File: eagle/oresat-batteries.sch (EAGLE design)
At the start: 308 parts, among them J1 J-SAMTEC-TFM-120-X1-XXX-D-RA, J4 ORESAT-DEBUG-CONNECTOR-ALL, Q1 DMP2240UDM, Q10 NTR4101, Q11 PMV45EN, Q12 Si7625DN, Q13 Si7625DN, Q14 NTR4101, Q15 NTR4101, Q16 Si7625DN, Q17 Si7625DN, Q18 Si7625DN, Q19 Si7625DN, Q2 PMV45EN, Q22 PMV45EN, Q23 NTR4101, Q24 PM45VEN, Q25 PM45VEN, Q26 PM45VEN, Q27 PM45VEN, Q28 NTR4101, Q29 PM45VEN, Q3 DMP3050LVT-7, Q30 Si7625DN, Q31 Si7625DN, Q32 NTR4101, Q33 NTR4101, Q34 Si7625DN, Q35 Si7625DN, Q36 Si7625DN, Q37 Si7625DN, Q4 DMP3050LVT-7, Q40 PM45VEN, Q41 NTR4101, Q42 DMP2240UDM, Q43 DMP2240UDM, Q44 PMV45EN, Q45 FDMQ86530L_2-GATES, Q5 PMV45EN, Q6 PM45VEN, Q7 PM45VEN, Q8 PM45VEN, Q9 PM45VEN, U1 MAX7310ATE, U10 LTC4412, U11 LTC4412, U12 MAX17205G, U13 S-8209AAA-T8T1U, U14 S-8209AAA-T8T1U, U15 LTC4412, U16 LTC4412, U17 MAX17205G, U2 MIC842LYC5, U20 TCAN330, U21 STM32F091C, U3 MIC842LYC5, U4 MAX4211FETE, U5 TPS62111RSA, U8 S-8209AAA-T8T1U, U9 S-8209AAA-T8T1U, X3 16MHZ-2.5x2mm

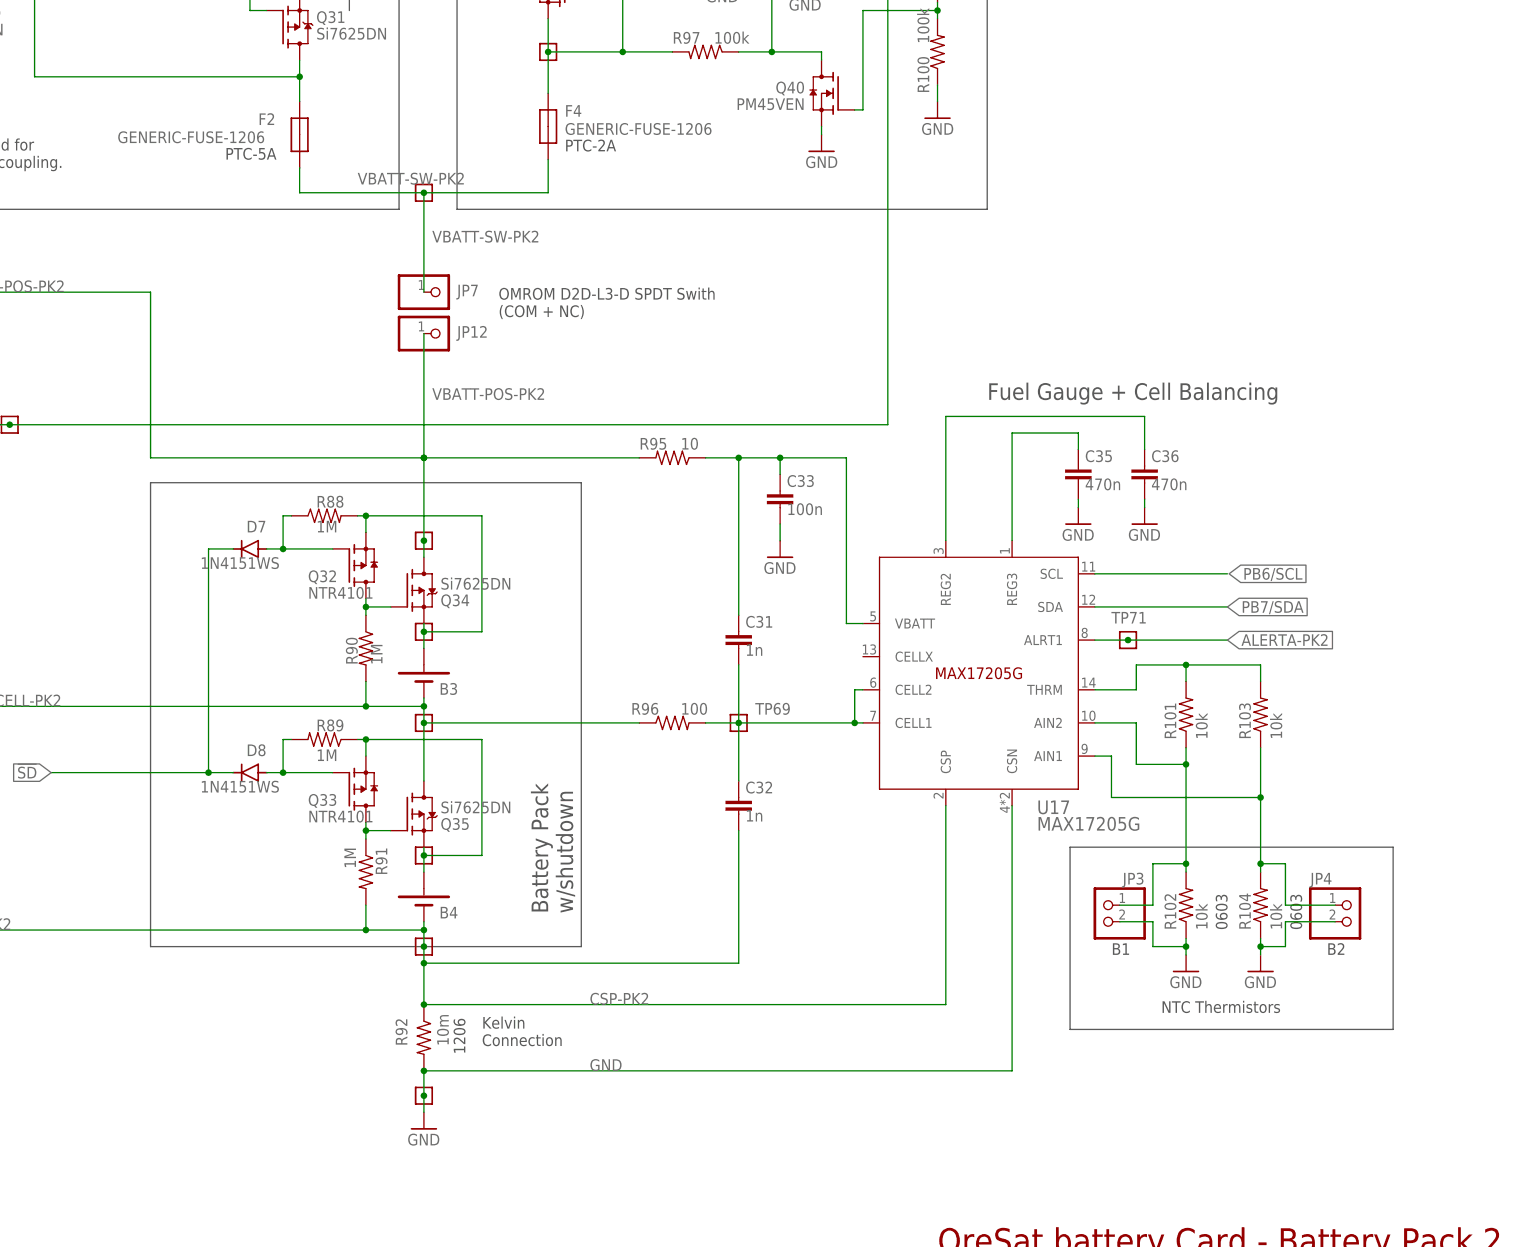
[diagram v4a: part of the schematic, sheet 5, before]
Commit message: Full update of the BOM; added non PCB materials including the heaters, thermistors. Updated fuses to be decent PTCs. Might regret that later, but it really seems like the right thing.
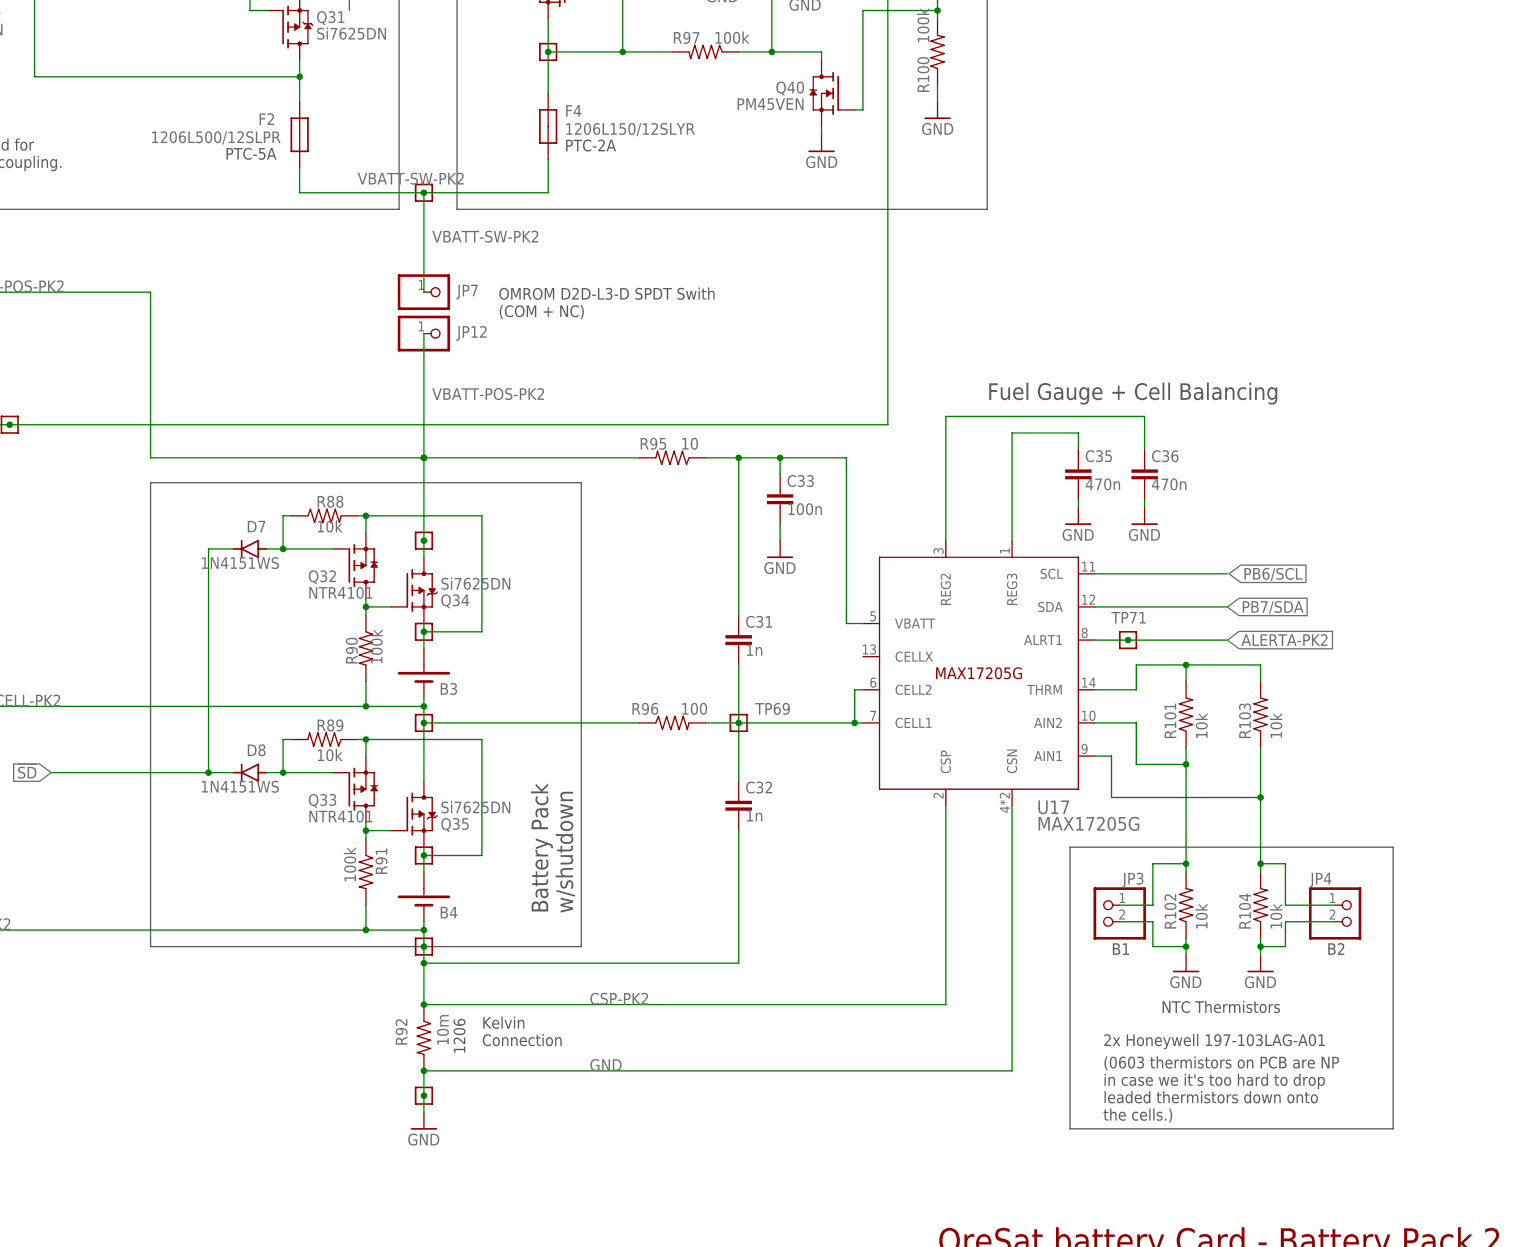
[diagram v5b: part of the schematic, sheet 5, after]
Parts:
- C7: value NP -> 1u
- F1, F2: value GENERIC-FUSE-1206 -> 1206L500/12SLPR
- F3, F4: value GENERIC-FUSE-1206 -> 1206L150/12SLYR
- R26: value NP -> 100k
- R27: value NP -> 10k
- R88, R89: value 1M -> 10k
- R90, R91: value 1M -> 100k
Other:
- note added: "(0603 thermistors on PCB are NP in case we it's too hard to drop leaded thermistors down onto the cells.)"
- note added: "2x Honeywell 197-103LAG-A01"
- note removed: "0603"
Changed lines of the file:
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@@
 <part name="TP41" library="oresat-misc" deviceset="TEST-POINT-LARGE-SQUARE" device=""/>
 <part name="TP39" library="oresat-misc" deviceset="TEST-POINT-LARGE-SQUARE" device=""/>
-<part name="F1" library="F-Generic-Fuse-1206" deviceset="GENERIC-FUSE-1206" device="">
+<part name="F1" library="F-Generic-Fuse-1206" deviceset="GENERIC-FUSE-1206" device="" value="1206L500/12SLPR">
 <attribute name="DIS" value="Digi-Key"/>
 <attribute name="DPN" value="F9966CT-ND"/>
@@
 <attribute name="MPN" value="S-8209AAA-T8T1U"/>
 </part>
-<part name="R91" library="oresat-rcl" deviceset="R-US_" device="0603-C-NOSILK" value="1M">
+<part name="R91" library="oresat-rcl" deviceset="R-US_" device="0603-C-NOSILK" value="100k">
 <attribute name="DIS" value="Digi-Key"/>
 <attribute name="DPN" value="311-1.00MHRCT-ND"/>
@@
 <attribute name="MPN" value="RC0603FR-071ML"/>
 </part>
-<part name="R90" library="oresat-rcl" deviceset="R-US_" device="0603-C-NOSILK" value="1M">
+<part name="R90" library="oresat-rcl" deviceset="R-US_" device="0603-C-NOSILK" value="100k">
 <attribute name="DIS" value="Digi-Key"/>
 <attribute name="DPN" value="311-1.00MHRCT-ND"/>
@@
 <attribute name="MPN" value="1N4151WS-E3-08"/>
 </part>
-<part name="R89" library="oresat-rcl" deviceset="R-US_" device="0603-C-NOSILK" value="1M">
+<part name="R89" library="oresat-rcl" deviceset="R-US_" device="0603-C-NOSILK" value="10k">
 <attribute name="DIS" value="Digi-Key"/>
 <attribute name="DPN" value="311-1.00MHRCT-ND"/>
@@
 <attribute name="MPN" value="RC0603FR-071ML"/>
 </part>
-<part name="R88" library="oresat-rcl" deviceset="R-US_" device="0603-C-NOSILK" value="1M">
+<part name="R88" library="oresat-rcl" deviceset="R-US_" device="0603-C-NOSILK" value="10k">
 <attribute name="DIS" value="Digi-Key"/>
 <attribute name="DPN" value="311-1.00MHRCT-ND"/>
@@
 <part name="TP64" library="oresat-misc" deviceset="TEST-POINT-LARGE-SQUARE" device=""/>
 <part name="TP62" library="oresat-misc" deviceset="TEST-POINT-LARGE-SQUARE" device=""/>
-<part name="F2" library="F-Generic-Fuse-1206" deviceset="GENERIC-FUSE-1206" device="">
+<part name="F2" library="F-Generic-Fuse-1206" deviceset="GENERIC-FUSE-1206" device="" value="1206L500/12SLPR">
 <attribute name="DIS" value="Digi-Key"/>
 <attribute name="DPN" value="F9966CT-ND"/>
@@
 <attribute name="MPN" value="RC0603FR-0710KL"/>
 </part>
-<part name="R26" library="oresat-rcl" deviceset="R-US_" device="0603-C-NOSILK" value="NP">
+<part name="R26" library="oresat-rcl" deviceset="R-US_" device="0603-C-NOSILK" value="100k">
 <attribute name="DIS" value="Digi-Key"/>
 <attribute name="DPN" value="1276-4275-1-ND"/>
@@
 <attribute name="MPN" value="RC1005F6653CS"/>
 </part>
-<part name="R27" library="oresat-rcl" deviceset="R-US_" device="0603-C-NOSILK" value="NP">
+<part name="R27" library="oresat-rcl" deviceset="R-US_" device="0603-C-NOSILK" value="10k">
 <attribute name="DIS" value="Digi-Key"/>
 <attribute name="DPN" value="1276-4275-1-ND"/>
@@
 </part>
 <part name="GND19" library="supply1" library_urn="urn:adsk.eagle:library:371" deviceset="GND" device=""/>
-<part name="C7" library="oresat-rcl" deviceset="C-EU" device="0603-C-NOSILK" value="NP"/>
+<part name="C7" library="oresat-rcl" deviceset="C-EU" device="0603-C-NOSILK" value="1u"/>
 <part name="GND28" library="supply1" library_urn="urn:adsk.eagle:library:371" deviceset="GND" device=""/>
 <part name="R38" library="oresat-rcl" deviceset="R-US_" device="0603-C-NOSILK" value="10k">
@@
 <part name="GND31" library="supply1" library_urn="urn:adsk.eagle:library:371" deviceset="GND" device=""/>
 <part name="GND32" library="supply1" library_urn="urn:adsk.eagle:library:371" deviceset="GND" device=""/>
-<part name="F3" library="F-Generic-Fuse-1206" deviceset="GENERIC-FUSE-1206" device="">
+<part name="F3" library="F-Generic-Fuse-1206" deviceset="GENERIC-FUSE-1206" device="" value="1206L150/12SLYR">
 <attribute name="DIS" value="Digi-Key"/>
 <attribute name="DPN" value="F9966CT-ND"/>
@@
 </part>
 <part name="PCB1" library="oresat-cards" deviceset="ORESAT-CARD-V1.3-BATTERY" device=""/>
-<part name="F4" library="F-Generic-Fuse-1206" deviceset="GENERIC-FUSE-1206" device="">
+<part name="F4" library="F-Generic-Fuse-1206" deviceset="GENERIC-FUSE-1206" device="" value="1206L150/12SLYR">
 <attribute name="DIS" value="Digi-Key"/>
 <attribute name="DPN" value="F9966CT-ND"/>
@@
 <text x="267.97" y="30.48" size="1.778" layer="97" rot="R270">-Y HEATER</text>
 <text x="288.29" y="31.75" size="1.778" layer="97" rot="R270">+Y HEATER</text>
-<text x="232.41" y="12.7" size="1.778" layer="97">2x Minco HK6903 Heaters (12.7 x 101.6 mm @ 49 ohm)</text>
+<text x="247.65" y="12.7" size="1.778" layer="97">2x Minco HK6903 Heaters (12.7 x 101.6 mm @ 49 ohm)</text>
 <wire x1="275.59" y1="52.07" x2="262.89" y2="52.07" width="0.1524" layer="97"/>
 <wire x1="262.89" y1="52.07" x2="262.89" y2="16.51" width="0.1524" layer="97"/>
@@
 <wire x1="214.63" y1="73.66" x2="280.67" y2="73.66" width="0.1524" layer="97"/>
 <text x="262.89" y="55.88" size="1.778" layer="97" rot="R90">1206</text>
-<text x="391.16" y="76.2" size="1.778" layer="97" rot="R90">0603</text>
-<text x="379.73" y="76.2" size="1.778" layer="97" rot="R90">0603</text>
-<wire x1="355.6" y1="88.9" x2="355.6" y2="60.96" width="0.1524" layer="97"/>
-<wire x1="355.6" y1="60.96" x2="405.13" y2="60.96" width="0.1524" layer="97"/>
-<wire x1="405.13" y1="60.96" x2="405.13" y2="88.9" width="0.1524" layer="97"/>
+<wire x1="355.6" y1="88.9" x2="355.6" y2="44.45" width="0.1524" layer="97"/>
+<wire x1="355.6" y1="44.45" x2="405.13" y2="44.45" width="0.1524" layer="97"/>
+<wire x1="405.13" y1="44.45" x2="405.13" y2="88.9" width="0.1524" layer="97"/>
 <wire x1="405.13" y1="88.9" x2="355.6" y2="88.9" width="0.1524" layer="97"/>
 <text x="369.57" y="63.5" size="1.778" layer="97">NTC Thermistors </text>
@@
 <text x="266.7" y="166.37" size="1.778" layer="97">OMRON D2D-L3-D SPDT Switch
 (COM + NC)</text>
+<text x="360.68" y="46.99" size="1.778" layer="97">(0603 thermistors on PCB are NP
+in case we it's too hard to drop
+leaded thermistors down onto
+the cells.)</text>
+<text x="360.68" y="59.69" size="1.778" layer="97">2x Honeywell 197-103LAG-A01</text>
 </plain>
 <instances>
@@
 <instance part="F1" gate="G$1" x="237.49" y="198.12" smashed="yes" rot="R90">
 <attribute name="NAME" x="232.41" y="200.66" size="1.778" layer="95"/>
-<attribute name="VALUE" x="210.82" y="197.358" size="1.778" layer="96"/>
+<attribute name="VALUE" x="214.63" y="197.358" size="1.778" layer="96"/>
 <attribute name="DPN" x="237.49" y="198.12" size="1.778" layer="96" rot="R90" display="off"/>
 <attribute name="MFR" x="237.49" y="198.12" size="1.778" layer="96" rot="R90" display="off"/>
@@
 <wire x1="214.63" y1="73.66" x2="280.67" y2="73.66" width="0.1524" layer="97"/>
 <text x="262.89" y="57.15" size="1.778" layer="97" rot="R90">1206</text>
-<text x="391.16" y="76.2" size="1.778" layer="97" rot="R90">0603</text>
-<text x="379.73" y="76.2" size="1.778" layer="97" rot="R90">0603</text>
-<wire x1="355.6" y1="88.9" x2="355.6" y2="60.96" width="0.1524" layer="97"/>
-<wire x1="355.6" y1="60.96" x2="405.13" y2="60.96" width="0.1524" layer="97"/>
-<wire x1="405.13" y1="60.96" x2="405.13" y2="88.9" width="0.1524" layer="97"/>
+<wire x1="355.6" y1="88.9" x2="355.6" y2="45.72" width="0.1524" layer="97"/>
+<wire x1="355.6" y1="45.72" x2="405.13" y2="45.72" width="0.1524" layer="97"/>
+<wire x1="405.13" y1="45.72" x2="405.13" y2="88.9" width="0.1524" layer="97"/>
 <wire x1="405.13" y1="88.9" x2="355.6" y2="88.9" width="0.1524" layer="97"/>
 <text x="369.57" y="63.5" size="1.778" layer="97">NTC Thermistors </text>
@@
 <text x="267.97" y="170.18" size="1.778" layer="97">OMROM D2D-L3-D SPDT Swith
 (COM + NC)</text>
+<text x="360.68" y="46.99" size="1.778" layer="97">(0603 thermistors on PCB are NP
+in case we it's too hard to drop
+leaded thermistors down onto
+the cells.)</text>
+<text x="360.68" y="58.42" size="1.778" layer="97">2x Honeywell 197-103LAG-A01</text>
 </plain>
 <instances>
@@
 <instance part="F2" gate="G$1" x="237.49" y="198.12" smashed="yes" rot="R90">
 <attribute name="NAME" x="231.14" y="199.6186" size="1.778" layer="95"/>
-<attribute name="VALUE" x="209.55" y="196.85" size="1.778" layer="96"/>
+<attribute name="VALUE" x="214.63" y="196.85" size="1.778" layer="96"/>
 <attribute name="MPN" x="237.49" y="198.12" size="1.778" layer="96" rot="R90" display="off"/>
 <attribute name="DPN" x="237.49" y="198.12" size="1.778" layer="96" rot="R90" display="off"/>

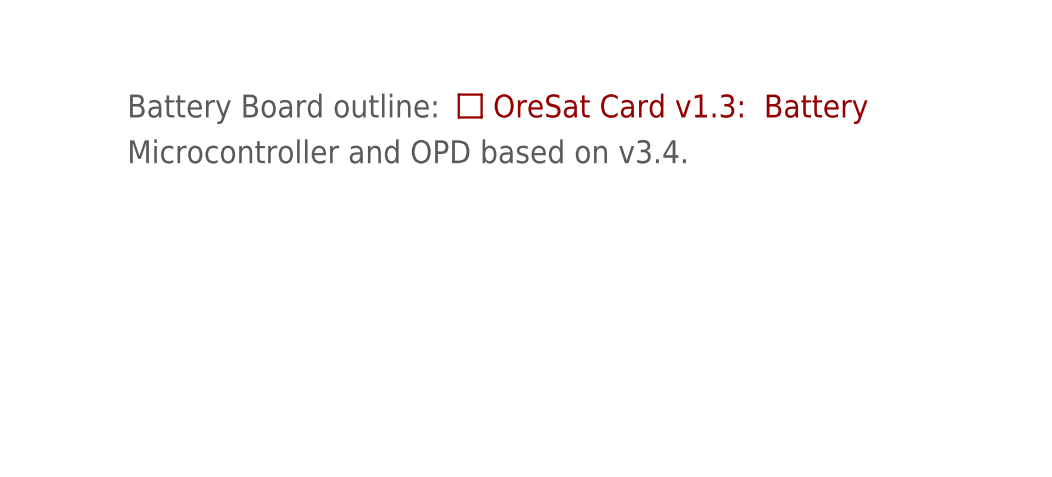
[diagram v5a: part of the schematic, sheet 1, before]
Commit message: Upped battery board to v2.1. No real changes, besides adding fiducials (blargh!), updating the board version, and adding the flight marker to TPLACE.
More importantly, the BOM has been upadated to reflect what Screaming Circuits is going to stuff for us.
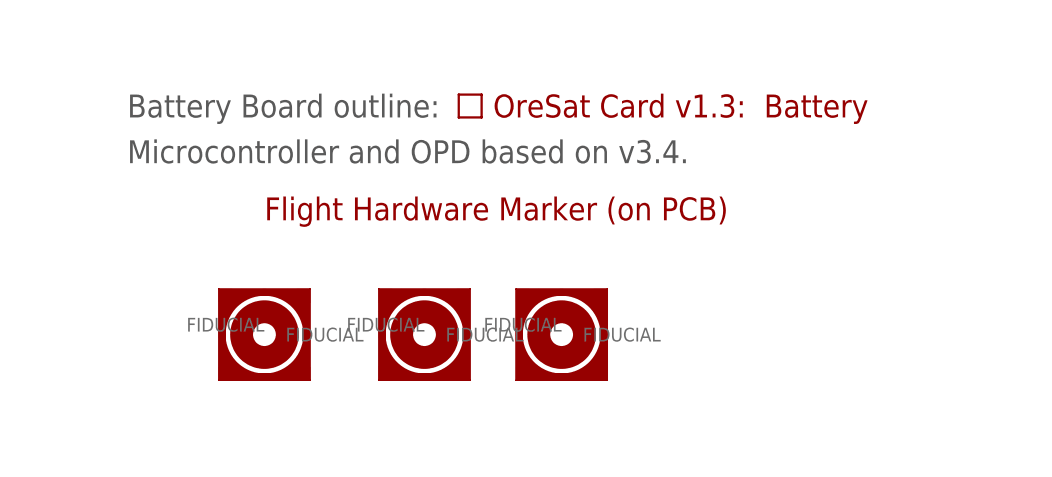
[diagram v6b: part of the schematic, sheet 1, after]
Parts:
- added FIDUCIAL1, FIDUCIAL2, FIDUCIAL3: FIDUCIAL-1.0X2.0, dock_v2:FIDUCIAL-1.0X2.0
- added U$1: FLIGHMARKERNEW, oresat-flight-marker:FLIGHMARKERNEW
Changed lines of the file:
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@@
 <setting verticaltext="up"/>
 </settings>
-<grid distance="0.05" unitdist="inch" unit="inch" style="lines" multiple="2" display="no" altdistance="0.01" altunitdist="inch" altunit="inch"/>
+<grid distance="0.1" unitdist="inch" unit="inch" style="lines" multiple="1" display="no" altdistance="0.01" altunitdist="inch" altunit="inch"/>
 <layers>
 <layer number="1" name="Top" color="4" fill="1" visible="no" active="no"/>
@@
 <attribute name="MPN" value="NANOSMD350LR-C-2"/>
 </part>
+<part name="FIDUCIAL1" library="dock_v2" deviceset="FIDUCIAL" device="-1.0X2.0"/>
+<part name="FIDUCIAL2" library="dock_v2" deviceset="FIDUCIAL" device="-1.0X2.0"/>
+<part name="FIDUCIAL3" library="dock_v2" deviceset="FIDUCIAL" device="-1.0X2.0"/>
+<part name="U$1" library="oresat-flight-marker" deviceset="FLIGHMARKER" device="NEW"/>
 </parts>
 <sheets>
@@
 </instance>
 <instance part="PCB1" gate="G$1" x="157.48" y="40.64" smashed="yes"/>
+<instance part="FIDUCIAL1" gate="FIDUCIAL" x="134.62" y="15.24" smashed="yes"/>
+<instance part="FIDUCIAL2" gate="FIDUCIAL" x="152.4" y="15.24" smashed="yes"/>
+<instance part="FIDUCIAL3" gate="FIDUCIAL" x="167.64" y="15.24" smashed="yes"/>
+<instance part="U$1" gate="G$1" x="134.62" y="27.94" smashed="yes"/>
 </instances>
 <busses>
